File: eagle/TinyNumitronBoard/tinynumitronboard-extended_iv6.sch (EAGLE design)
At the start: 32 parts

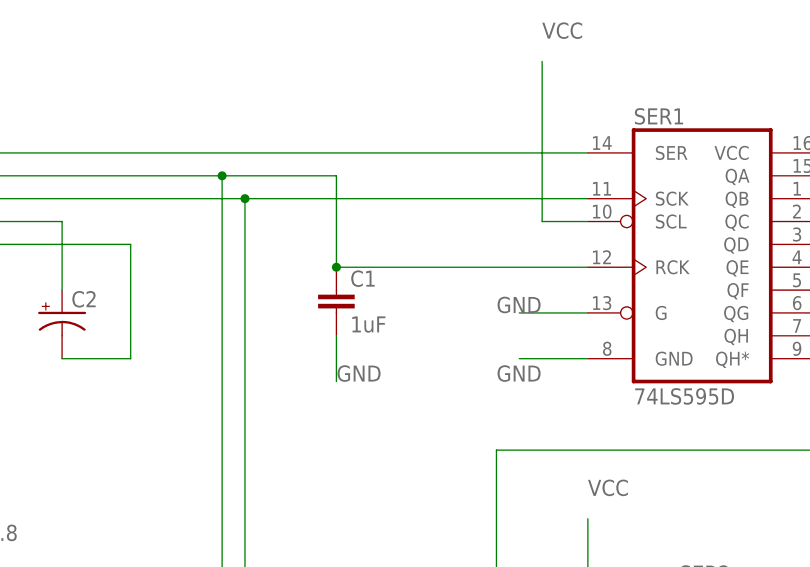
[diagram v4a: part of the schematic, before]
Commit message: Added cap for CLK
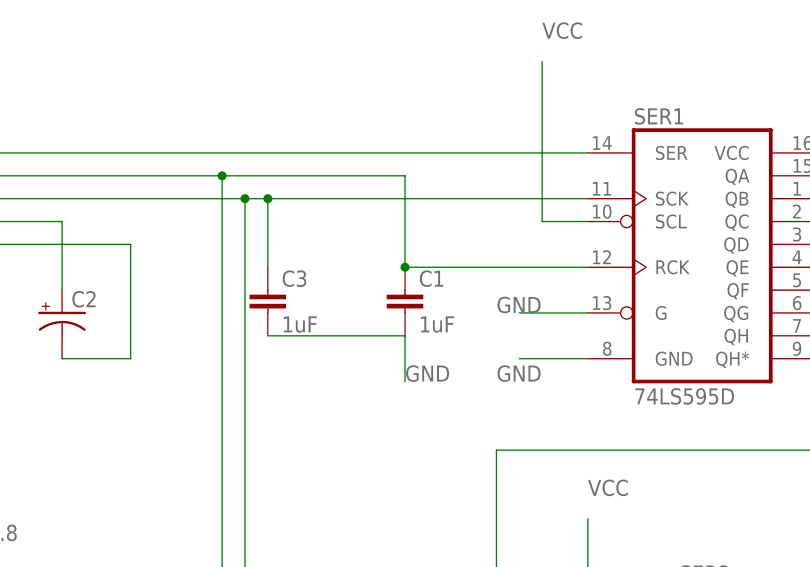
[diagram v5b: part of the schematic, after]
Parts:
- added C3: 1uF, resistor:C-EUC1206
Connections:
- net GND: now also C3.2
- net SCK: now also C3.1
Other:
- moved on the sheet: C1
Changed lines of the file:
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@@
 <part name="J1" library="SparkFun-Connectors" deviceset="CONN_02" device="1X02_NO_SILK"/>
 <part name="J2" library="SparkFun-Connectors" deviceset="CONN_02" device="1X02_NO_SILK"/>
+<part name="C3" library="resistor" deviceset="C-EU" device="C1206" value="1uF"/>
 </parts>
 <sheets>
@@
 </plain>
 <instances>
-<instance part="C1" gate="G$1" x="-88.9" y="48.26"/>
+<instance part="C1" gate="G$1" x="-81.28" y="48.26"/>
 <instance part="H4" gate="G$1" x="-144.78" y="22.86"/>
 <instance part="H1" gate="G$1" x="-144.78" y="17.78"/>
@@
 <instance part="J1" gate="G$1" x="111.76" y="86.36" rot="R270"/>
 <instance part="J2" gate="G$1" x="111.76" y="-144.78" rot="R270"/>
+<instance part="C3" gate="G$1" x="-96.52" y="48.26"/>
 </instances>
 <busses>
@@
 <segment>
 <pinref part="C1" gate="G$1" pin="2"/>
-<wire x1="-88.9" y1="43.18" x2="-88.9" y2="38.1" width="0.1524" layer="91"/>
-<label x="-88.9" y="38.1" size="1.778" layer="95"/>
+<wire x1="-81.28" y1="43.18" x2="-81.28" y2="38.1" width="0.1524" layer="91"/>
+<label x="-81.28" y="38.1" size="1.778" layer="95"/>
+<pinref part="C3" gate="G$1" pin="2"/>
+<wire x1="-96.52" y1="43.18" x2="-81.28" y2="43.18" width="0.1524" layer="91"/>
 </segment>
 <segment>
@@
 <pinref part="SER2" gate="A" pin="SCK"/>
 <wire x1="-142.24" y1="58.42" x2="-99.06" y2="58.42" width="0.1524" layer="91"/>
-<wire x1="-99.06" y1="58.42" x2="-60.96" y2="58.42" width="0.1524" layer="91"/>
+<wire x1="-99.06" y1="58.42" x2="-96.52" y2="58.42" width="0.1524" layer="91"/>
+<wire x1="-96.52" y1="58.42" x2="-60.96" y2="58.42" width="0.1524" layer="91"/>
 <wire x1="-99.06" y1="58.42" x2="-99.06" y2="7.62" width="0.1524" layer="91"/>
 <wire x1="-99.06" y1="7.62" x2="-99.06" y2="-50.8" width="0.1524" layer="91"/>
@@
 <pinref part="JP_INPUT" gate="G$1" pin="3"/>
 <pinref part="JP_OUTPUT" gate="G$1" pin="3"/>
+<pinref part="C3" gate="G$1" pin="1"/>
+<wire x1="-96.52" y1="50.8" x2="-96.52" y2="58.42" width="0.1524" layer="91"/>
+<junction x="-96.52" y="58.42"/>
 </segment>
 </net>
@@
 <pinref part="SER2" gate="A" pin="RCK"/>
 <wire x1="-142.24" y1="60.96" x2="-101.6" y2="60.96" width="0.1524" layer="91"/>
-<wire x1="-101.6" y1="60.96" x2="-88.9" y2="60.96" width="0.1524" layer="91"/>
-<wire x1="-88.9" y1="60.96" x2="-88.9" y2="50.8" width="0.1524" layer="91"/>
+<wire x1="-101.6" y1="60.96" x2="-81.28" y2="60.96" width="0.1524" layer="91"/>
+<wire x1="-81.28" y1="60.96" x2="-81.28" y2="50.8" width="0.1524" layer="91"/>
 <pinref part="C1" gate="G$1" pin="1"/>
-<wire x1="-88.9" y1="50.8" x2="-60.96" y2="50.8" width="0.1524" layer="91"/>
-<junction x="-88.9" y="50.8"/>
+<wire x1="-81.28" y1="50.8" x2="-60.96" y2="50.8" width="0.1524" layer="91"/>
+<junction x="-81.28" y="50.8"/>
 <wire x1="-101.6" y1="60.96" x2="-101.6" y2="0" width="0.1524" layer="91"/>
 <wire x1="-101.6" y1="0" x2="-101.6" y2="-58.42" width="0.1524" layer="91"/>

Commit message: Final commit before sending v2.0 to production
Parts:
- J_LED_IN, J_LED_OUT: device SparkFun-Connectors:M01NOSILK-KIT -> SparkFun-Connectors:CONN_01
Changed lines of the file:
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@@
 <part name="D3" library="SparkFun-LED" deviceset="WS2812B" device=""/>
 <part name="D4" library="SparkFun-LED" deviceset="WS2812B" device=""/>
-<part name="J_LED_IN" library="SparkFun-Connectors" deviceset="M01" device="NOSILK-KIT"/>
-<part name="J_LED_OUT" library="SparkFun-Connectors" deviceset="M01" device="NOSILK-KIT"/>
+<part name="J_LED_IN" library="SparkFun-Connectors" deviceset="CONN_01" device=""/>
+<part name="J_LED_OUT" library="SparkFun-Connectors" deviceset="CONN_01" device=""/>
 <part name="TUBE2" library="kalshagar" deviceset="IV6_NUMITRON" device="LARGE" value="IV6_NUMITRONLARGE"/>
 <part name="SER2" library="SparkFun-DigitalIC" deviceset="74*595" device="D" technology="LS"/>
